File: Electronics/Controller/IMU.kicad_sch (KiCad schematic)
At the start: 0 parts

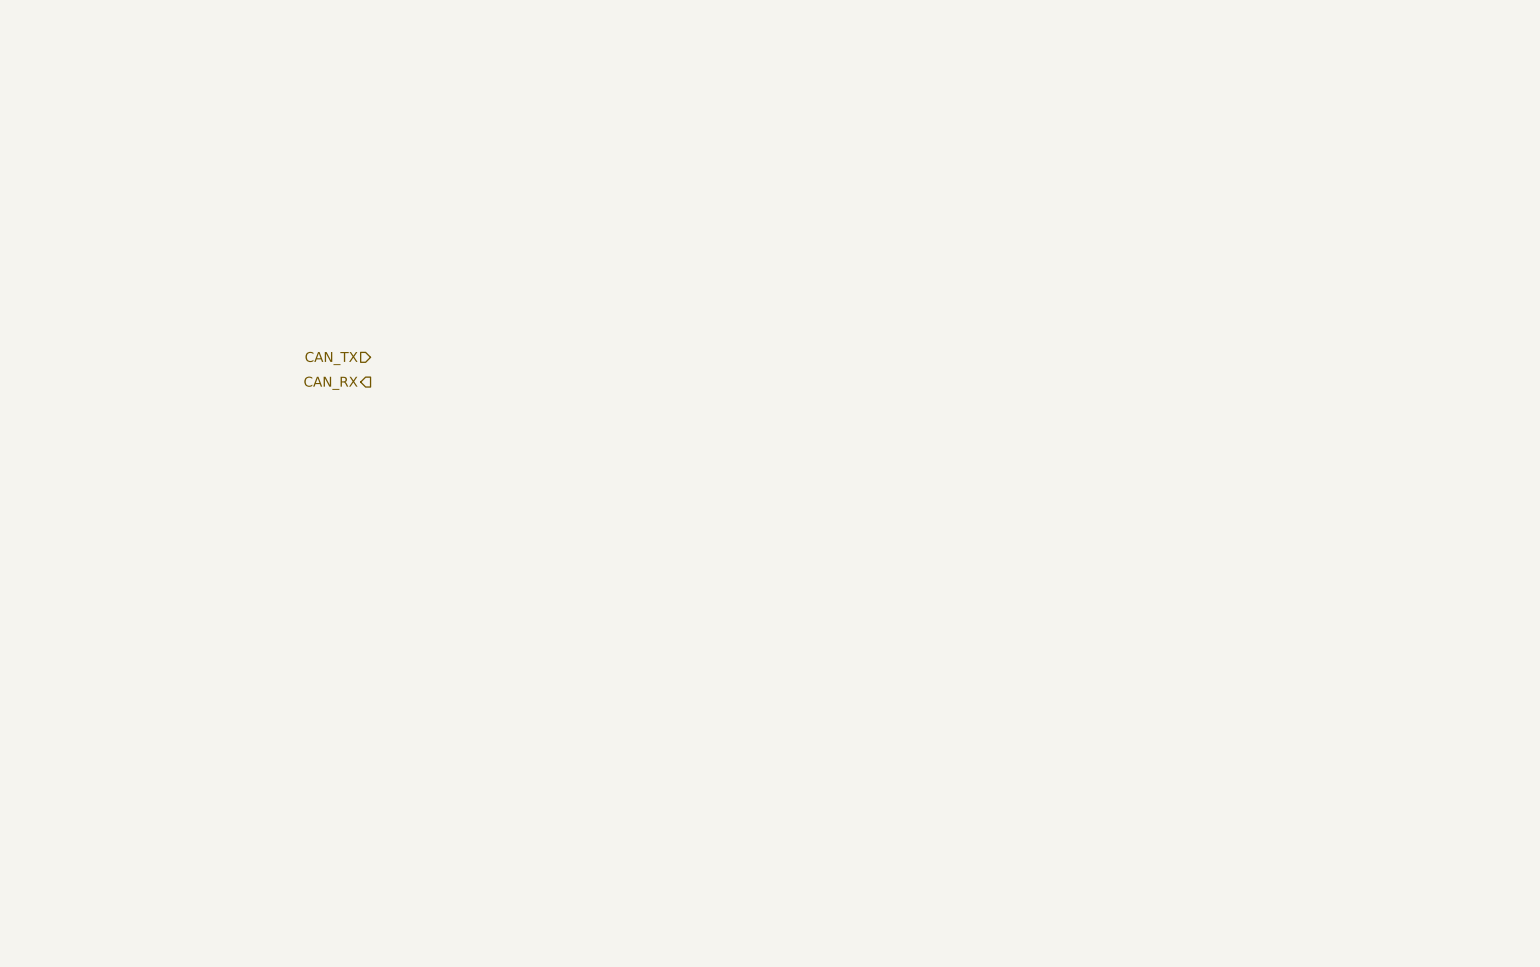
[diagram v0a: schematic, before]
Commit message: Working on schematic. Added datasheets.
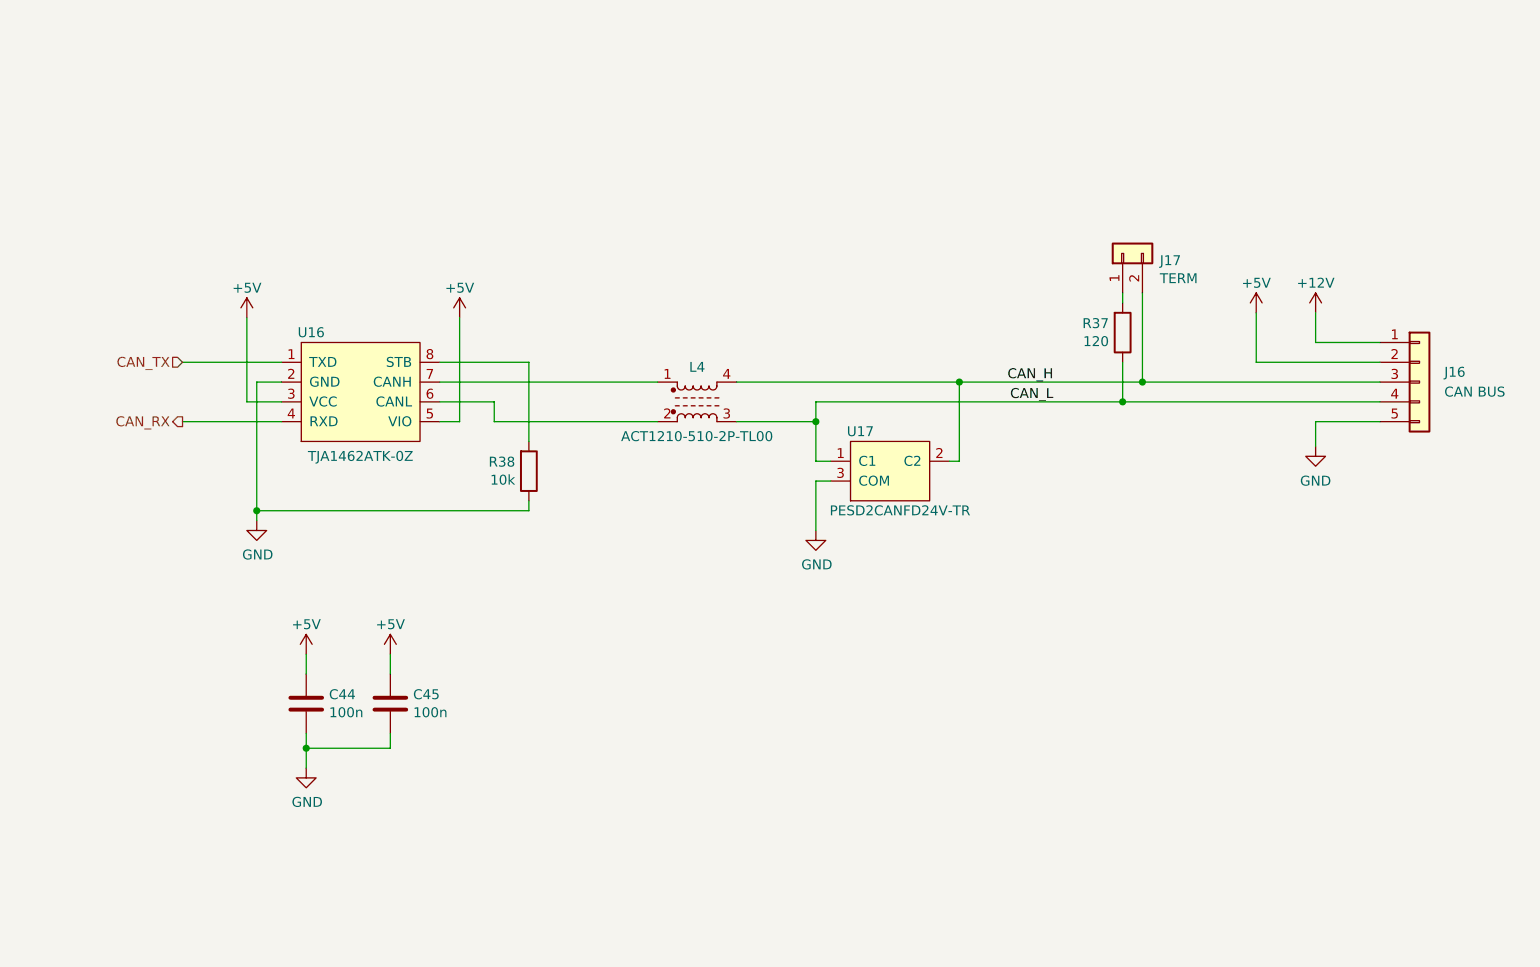
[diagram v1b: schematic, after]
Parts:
- added C44, C45: 100n, symbol Device:C
- added J16: CAN BUS, symbol Connector_Generic:Conn_01x05
- added J17: TERM, Connector_PinHeader_2.54mm:PinHeader_1x02_P2.54mm_Vertical, symbol Connector_Generic:Conn_01x02
- added L4: ACT1210-510-2P-TL00, EmSA:ACT1210-510-2P-TL00, symbol Device:L_Ferrite_Coupled_1423
- added R37: 120, symbol Device:R
- added R38: 10k, symbol Device:R
- added U16: TJA1462ATK-0Z, EmSA:HVSON8_0_65mm, symbol EmSA:TJA1462ATK
- added U17: PESD2CANFD24V-TR, Package_TO_SOT_SMD:SOT-23, symbol EmSA:PESD2CANFD24V-T
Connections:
- net CAN_RX: now also U16.4 (RXD)
- net CAN_TX: now also U16.1 (TXD)
- new net: J17.1 (Pin_1), R37.2
- new net: L4.1, U16.7 (CANH)
- new net: L4.2, U16.6 (CANL)
- new net: R38.2, U16.8 (STB)
- new net +12V: J16.1 (Pin_1)
- new net +5V: C44.1, C45.1, J16.2 (Pin_2), U16.3 (VCC), U16.5 (VIO)
- new net CAN_H: J16.3 (Pin_3), J17.2 (Pin_2), L4.4, U17.2 (C2)
- new net CAN_L: J16.4 (Pin_4), L4.3, R37.1, U17.1 (C1)
- new net GND: C44.2, C45.2, J16.5 (Pin_5), R38.1, U16.2 (GND), U17.3 (COM)

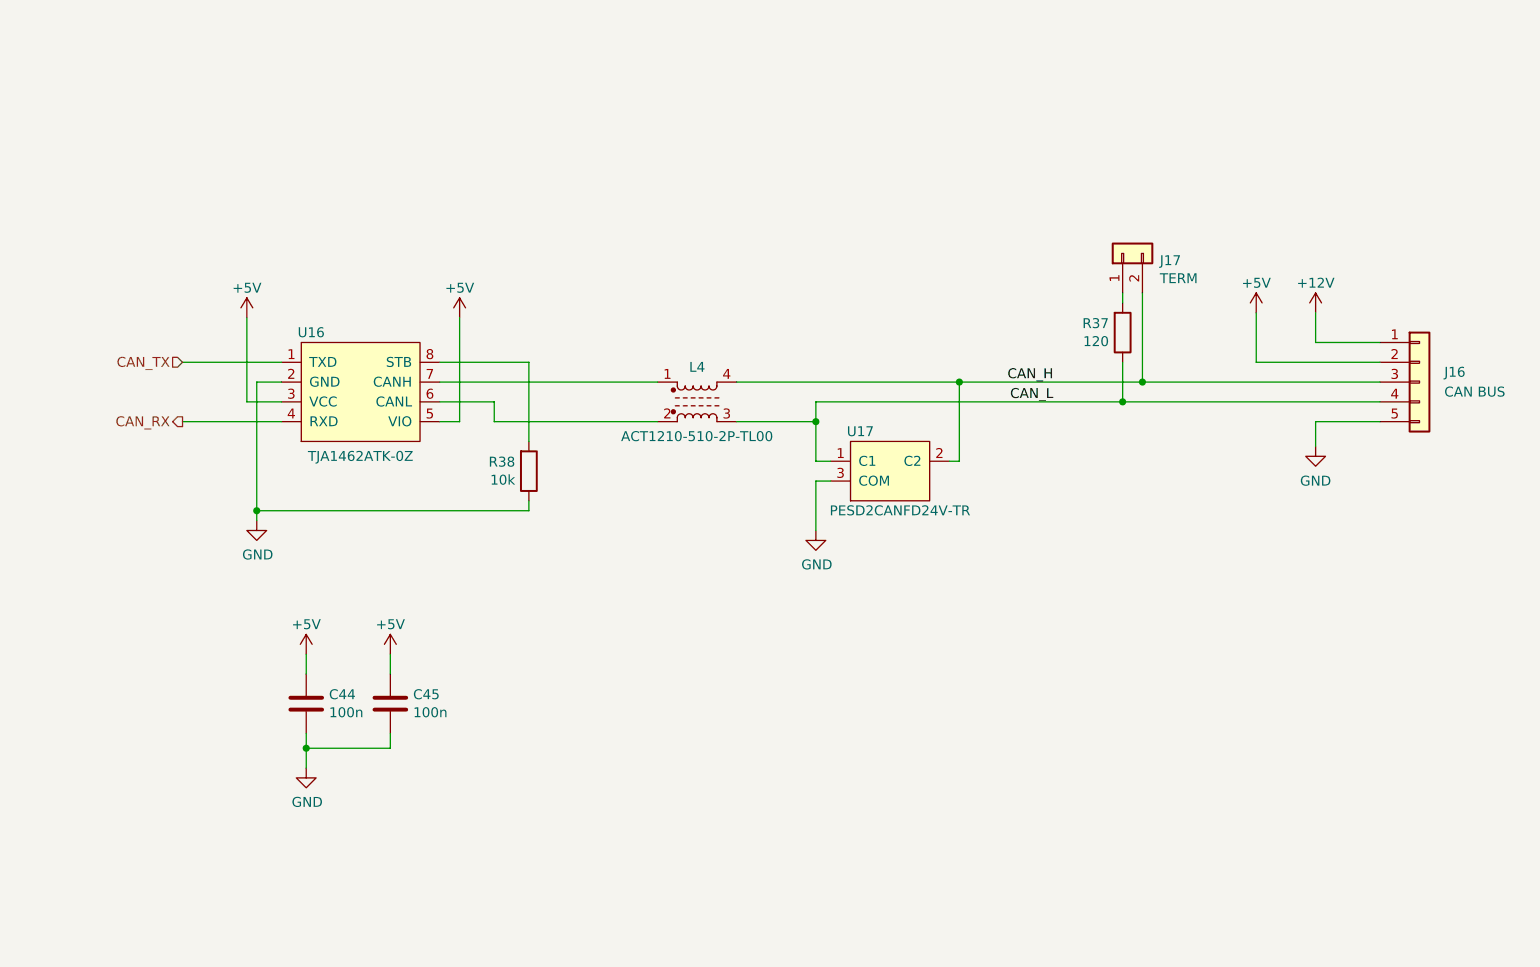
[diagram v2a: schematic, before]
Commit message: Updated schematic. Added footprints for all components.
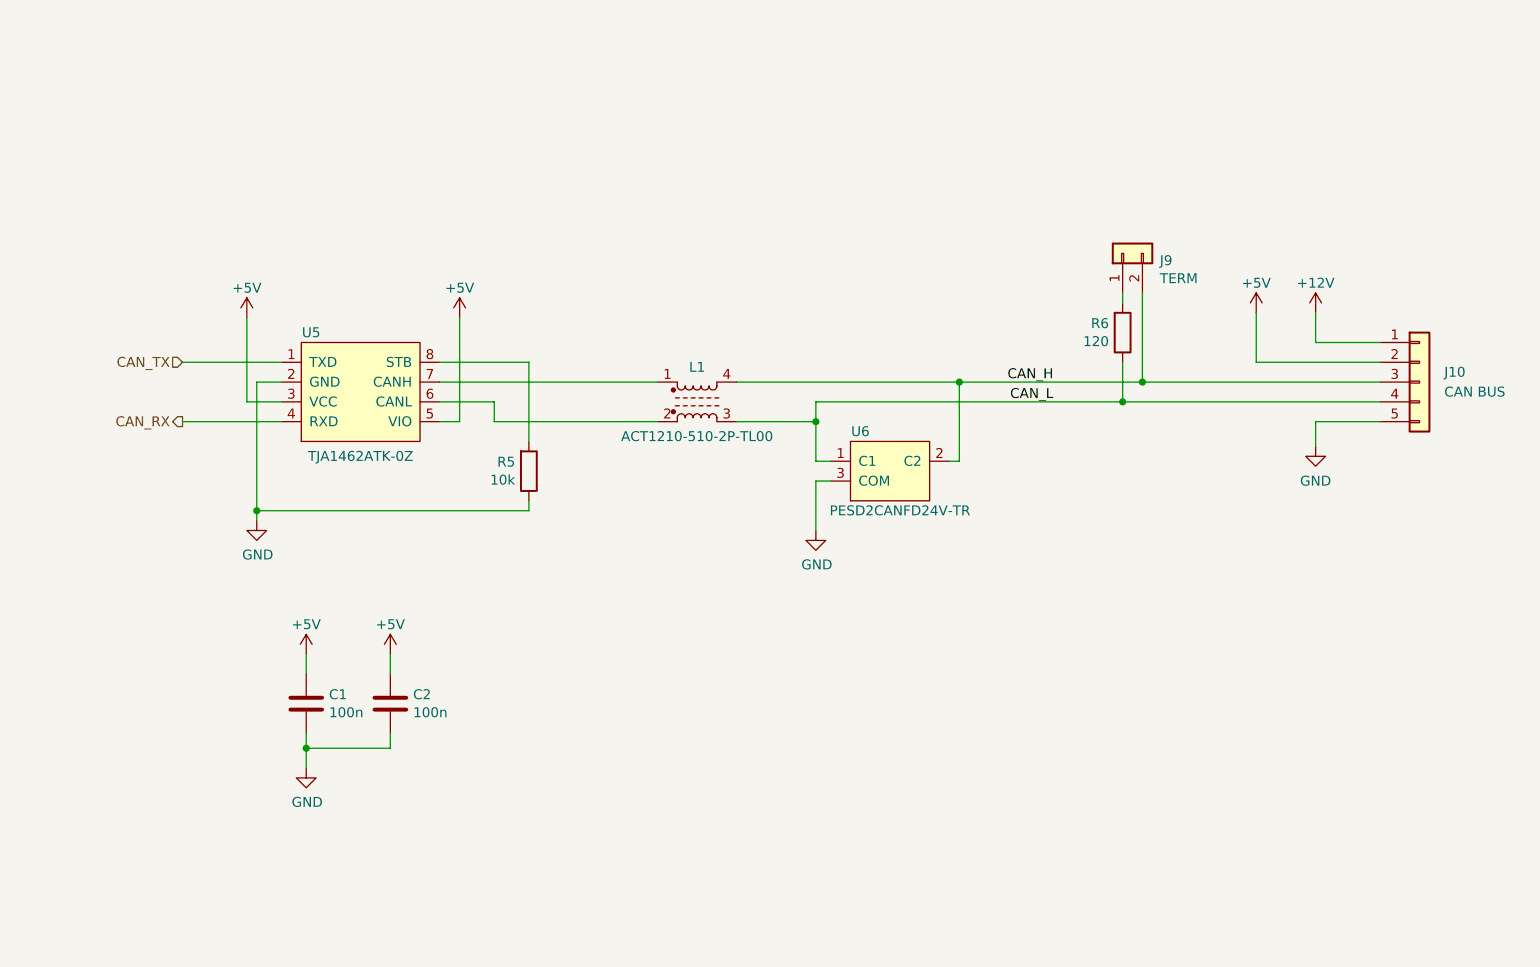
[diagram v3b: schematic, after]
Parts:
- C1: renamed from C44; footprint (none) -> Capacitor_SMD:C_0805_2012Metric
- C2: renamed from C45; footprint (none) -> Capacitor_SMD:C_0805_2012Metric
- J10: renamed from J16; footprint (none) -> Connector_JST:JST_PH_B5B-PH-K_1x05_P2.00mm_Vertical; manf# (none) -> B5B-PH-K-S
- R5: renamed from R38; footprint (none) -> Resistor_SMD:R_0805_2012Metric
- R6: renamed from R37; footprint (none) -> Resistor_SMD:R_0805_2012Metric
- renumbered J17 to J9, L4 to L1, U16 to U5, U17 to U6
